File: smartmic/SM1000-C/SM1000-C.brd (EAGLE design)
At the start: 65 x 90 mm, 176 parts, among them CN1 HDR100-3, CN10 MJ-3523-SMT, CN11 HDR100-3, CN12 DF11-16DS, CN2 MOLEX-MINI-B-SMT, CN3 RASM712PX, CN4 RJ-45, CN5 MJ-3523-SMT, CN6 MJ-3523-SMT, CN7 MJ-3523-SMT, CN8 MJ-3523-SMT, CN9 MJ-3523-SMT, J1 JMP-2PIN, J3 JMP-2PIN, J4 JMP-2PIN, J5 JMP-2PIN, P1 TPAD50, P10 TPAD50, P11 TPAD50, P12 TPAD50, P13 TPAD50, P14 TPAD50, P15 TPAD50, P16 TPAD50, P17 TPAD50, P18 TPAD50, P19 TPAD50, P2 TPAD50, P20 TPAD50, P3 TPAD50, P4 TPAD50, P5 TPAD50, P6 TPAD50, P7 TPAD50, P8 TPAD50, P9 TPAD50, SW1 SW-BOURNS-7914S, SW2 SW-BOURNS-7914S, SW3 DPDT, SW4 SW-BOURNS-7914S, T1 SM-LP-5001, T2 SM-LP-5001, U1 STM32F405, U2 LD3985M33R, U3 STMPS2141, U4 EMIF02-USB03F2, U5 TPS54329E, U6 LMV341, U7 LMV341, U8 LM386M-1, U9 LMV341

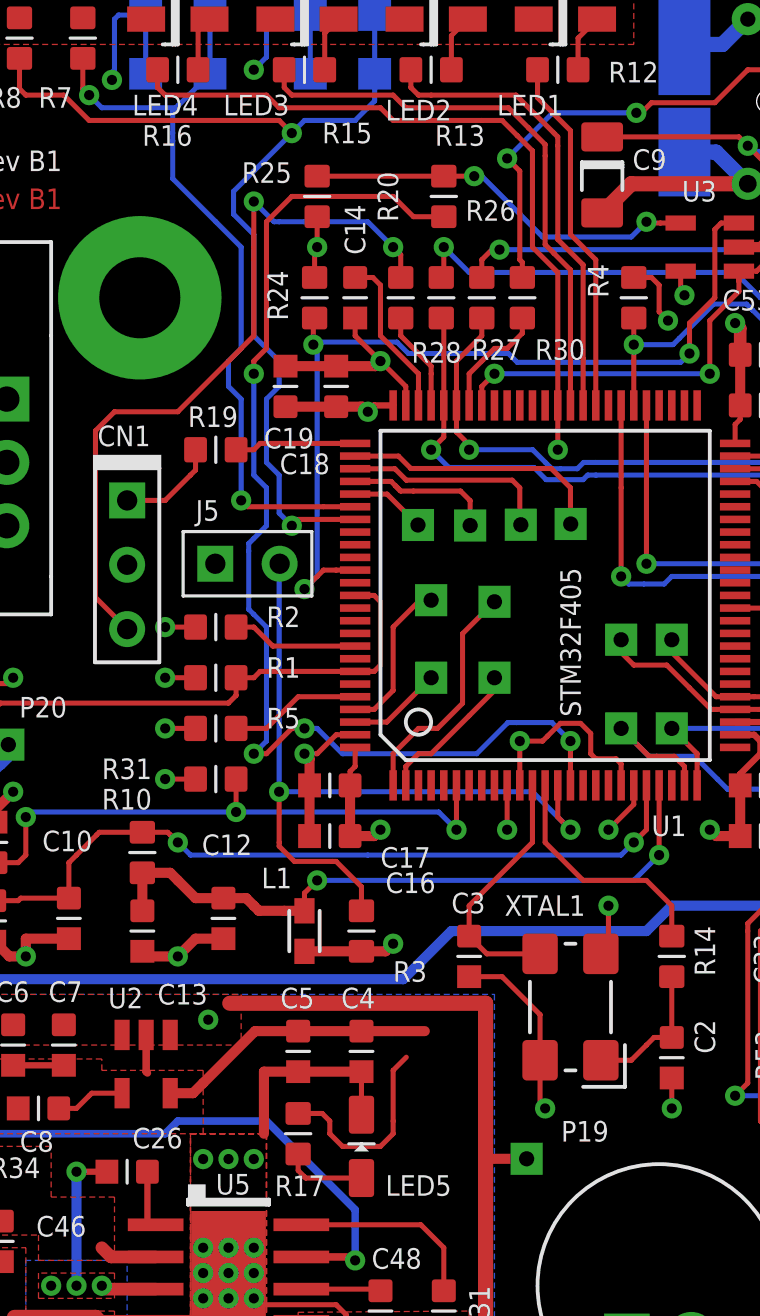
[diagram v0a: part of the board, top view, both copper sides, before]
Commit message: Verifying Change-Log-C items 1-15 RGB
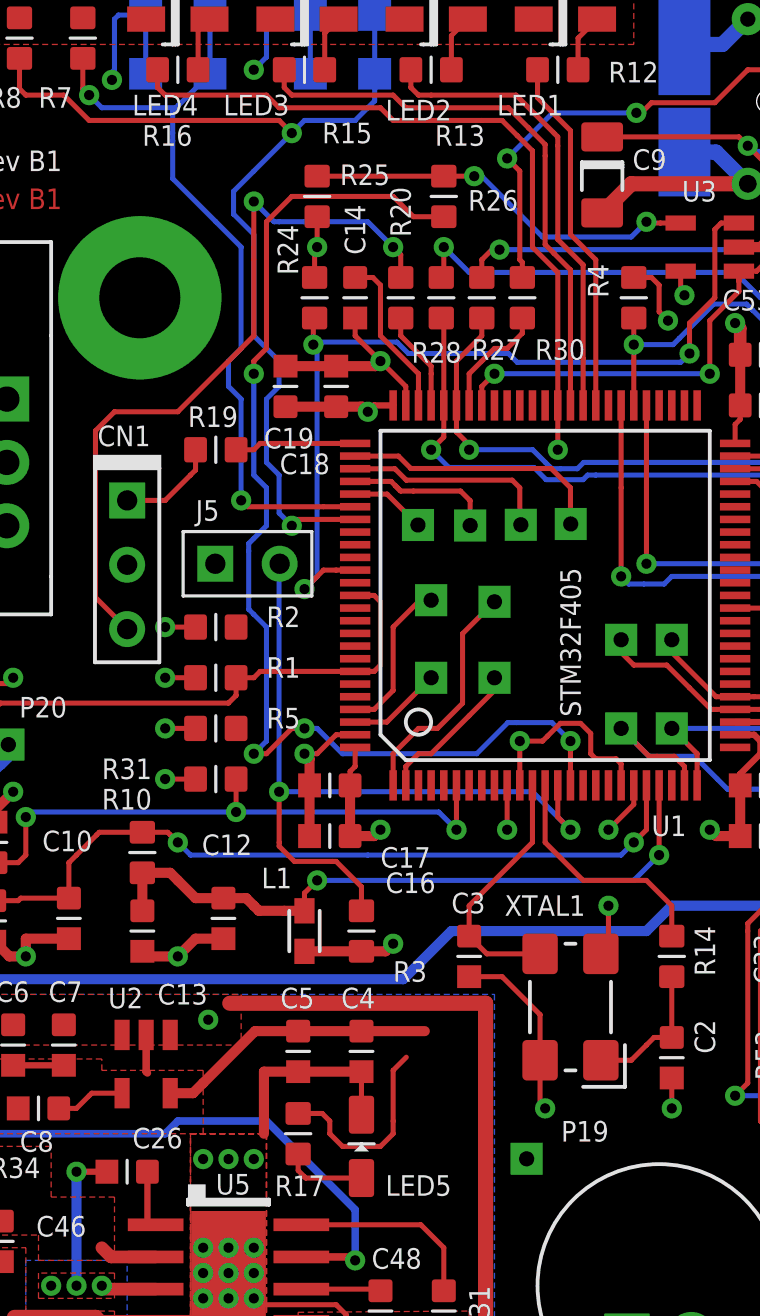
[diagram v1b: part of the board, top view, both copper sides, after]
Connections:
- removed net SCL: R2.2, U1.92
- removed net SDA: R5.2, U1.96
- net USART3_RX: now also R2.2
- net USART3_TX: now also R5.2
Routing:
- net SDA: track 5.22 -> 0.00 mm
- net SCL: track 5.01 -> 0.00 mm
- net +5V: track 96.6 -> 95.0 mm
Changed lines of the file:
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@@
 <layer number="14" name="Route14" color="1" fill="6" visible="no" active="no"/>
 <layer number="15" name="VDD" color="6" fill="1" visible="no" active="yes"/>
-<layer number="16" name="Bottom" color="1" fill="1" visible="yes" active="yes"/>
+<layer number="16" name="Bottom" color="1" fill="1" visible="no" active="yes"/>
 <layer number="17" name="Pads" color="2" fill="1" visible="yes" active="yes"/>
 <layer number="18" name="Vias" color="2" fill="1" visible="yes" active="yes"/>
@@
 <layer number="23" name="tOrigins" color="15" fill="1" visible="yes" active="yes"/>
 <layer number="24" name="bOrigins" color="15" fill="1" visible="no" active="yes"/>
-<layer number="25" name="tNames" color="7" fill="1" visible="no" active="yes"/>
+<layer number="25" name="tNames" color="7" fill="1" visible="yes" active="yes"/>
 <layer number="26" name="bNames" color="7" fill="1" visible="no" active="yes"/>
 <layer number="27" name="tValues" color="7" fill="1" visible="no" active="yes"/>
@@
 <layer number="203" name="BDIM" color="7" fill="1" visible="no" active="yes"/>
 <layer number="204" name="BRD-DIM" color="7" fill="1" visible="no" active="yes"/>
-<layer number="205" name="Speaker" color="7" fill="1" visible="yes" active="yes"/>
+<layer number="205" name="Speaker" color="7" fill="1" visible="no" active="yes"/>
 <layer number="250" name="Descript" color="3" fill="1" visible="no" active="no"/>
 <layer number="251" name="SMDround" color="12" fill="11" visible="no" active="no"/>
@@
 </element>
 <element name="R20" library="AA-ipc-7351-resistor" package="RESC1608X55N" value="22,1%" x="22.8" y="77.5" locked="yes" smashed="yes" rot="R90">
-<attribute name="NAME" x="22.7" y="80.5" size="0.8128" layer="25" rot="R90"/>
+<attribute name="NAME" x="23.2" y="79.9" size="0.8128" layer="25" rot="R90"/>
 </element>
 <element name="U2" library="_RoweTel" package="SOT23-5L" value="LD3985M33R" x="12.75" y="47.25" locked="yes" smashed="yes">
@@
 </element>
 <element name="R25" library="AA-ipc-7351-resistor" package="RESC1608X55N" value="10K,1%" x="19.5" y="81.5" locked="yes" smashed="yes" rot="R270">
-<attribute name="NAME" x="18.5" y="82.85" size="0.8128" layer="25" rot="R180"/>
+<attribute name="NAME" x="20.4" y="81.95" size="0.8128" layer="25"/>
 </element>
 <element name="R26" library="AA-ipc-7351-resistor" package="RESC1608X55N" value="0 Ohm" x="24.5" y="81.5" smashed="yes" rot="R90">
-<attribute name="NAME" x="25.361" y="80.539" size="0.8128" layer="25"/>
+<attribute name="NAME" x="25.461" y="80.939" size="0.8128" layer="25"/>
 </element>
 <element name="C9" library="_RoweTel" package="C1206-TANT" value="4.7uF,16V,TANT" x="30.75" y="82.35" locked="yes" smashed="yes" rot="R270">
@@
 </element>
 <element name="R24" library="AA-ipc-7351-resistor" package="RESC1608X55N" value="47K,1%" x="19.4" y="77.5" locked="yes" smashed="yes" rot="R270">
-<attribute name="NAME" x="18.35" y="76.6" size="0.8128" layer="25" rot="R90"/>
+<attribute name="NAME" x="18.75" y="78.4" size="0.8128" layer="25" rot="R90"/>
 </element>
 <element name="R46" library="_RoweTel" package="POT-3310C" value="100K" x="55.43" y="88.99" locked="yes" smashed="yes" rot="R90">
@@
 <wire x1="-30.3" y1="-49.5" x2="3.07" y2="6.26" width="0" layer="19" extent="1-1"/>
 </signal>
-<signal name="SCL">
-<contactref element="U1" pad="92"/>
-<contactref element="R2" pad="2"/>
-<wire x1="16.3" y1="64.5" x2="17" y2="64.5" width="0.2" layer="1"/>
-<wire x1="17" y1="64.5" x2="17.75" y2="63.75" width="0.2" layer="1"/>
-<wire x1="17.75" y1="63.75" x2="21" y2="63.75" width="0.2" layer="1"/>
-</signal>
-<signal name="SDA">
-<contactref element="U1" pad="96"/>
-<contactref element="R5" pad="2"/>
-<wire x1="21" y1="61.75" x2="18.75" y2="61.75" width="0.2" layer="1"/>
-<wire x1="18.75" y1="61.75" x2="17.5" y2="60.5" width="0.2" layer="1"/>
-<wire x1="17.5" y1="60.5" x2="16.3" y2="60.5" width="0.2" layer="1"/>
-</signal>
 <signal name="NRST">
 <contactref element="U1" pad="14"/>
@@
 <vertex x="1" y="1"/>
 </polygon>
-<contactref element="P19" pad="1"/>
 <wire x1="26.15" y1="43.5" x2="26.16" y2="43.51" width="0.4" layer="1"/>
-<wire x1="26.16" y1="43.51" x2="27.77" y2="43.51" width="0.4" layer="1"/>
 <wire x1="10.6" y1="49.65" x2="14.35" y2="49.65" width="0.4" layer="15"/>
 <via x="15.2" y="49" extent="1-16" drill="0.4"/>
 <wire x1="15.2" y1="49" x2="14.55" y2="49.65" width="0.4" layer="15"/>
 <wire x1="14.55" y1="49.65" x2="14.35" y2="49.65" width="0.4" layer="15"/>
+<contactref element="P19" pad="1"/>
+<wire x1="26.16" y1="43.51" x2="27.77" y2="43.51" width="0" layer="19" extent="1-1"/>
+<wire x1="15.2" y1="49" x2="16.05" y2="49.65" width="0" layer="19" extent="1-1"/>
+<wire x1="9.5" y1="48.8" x2="10.6" y2="49.65" width="0" layer="19" extent="1-15"/>
+<wire x1="13.7" y1="48.4" x2="14.35" y2="49.65" width="0" layer="19" extent="1-15"/>
+<wire x1="11.8" y1="48.4" x2="10.6" y2="49.65" width="0" layer="19" extent="1-15"/>
+<wire x1="7.5" y1="48.8" x2="9.5" y2="48.8" width="0" layer="19" extent="1-1"/>
+<wire x1="15.25" y1="28.25" x2="17.2" y2="29.5" width="0" layer="19" extent="1-1"/>
+<wire x1="5" y1="48.8" x2="7.5" y2="48.8" width="0" layer="19" extent="1-1"/>
+<wire x1="12.25" y1="28.25" x2="15.25" y2="28.25" width="0" layer="19" extent="1-1"/>
+<wire x1="15.3" y1="24.7" x2="15.25" y2="28.25" width="0" layer="19" extent="1-1"/>
+<wire x1="16.8" y1="24.7" x2="15.3" y2="24.7" width="0" layer="19" extent="1-1"/>
+<wire x1="10.8" y1="24.7" x2="12.25" y2="28.25" width="0" layer="19" extent="1-1"/>
+<wire x1="9.3" y1="24.7" x2="10.8" y2="24.7" width="0" layer="19" extent="1-1"/>
+<wire x1="5.95" y1="28.75" x2="9.3" y2="24.7" width="0" layer="19" extent="1-1"/>
 </signal>
 <signal name="N$12">
@@
 <wire x1="38.9" y1="68.9" x2="42.68" y2="68.9" width="0.2" layer="1"/>
 <wire x1="42.68" y1="68.9" x2="43.7" y2="69.92" width="0.2" layer="1"/>
+<contactref element="R2" pad="2"/>
+<wire x1="16.3" y1="64.5" x2="36" y2="70.75" width="0" layer="19" extent="1-1"/>
 </signal>
 <signal name="USART3_TX">
@@
 <wire x1="39.5" y1="68.4" x2="43.9" y2="68.4" width="0.2" layer="1"/>
 <wire x1="43.9" y1="68.4" x2="45" y2="69.5" width="0.2" layer="1"/>
+<contactref element="R5" pad="2"/>
+<wire x1="16.3" y1="60.5" x2="36" y2="70.25" width="0" layer="19" extent="1-1"/>
 </signal>
 <signal name="N$7">

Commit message: Update to reflect review of Change-Log-C.txt  RGB 09/08/2014
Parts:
- added C54: 1nF,16V, AA-ipc-7351-capacitor:CAPC1608X92N
- added R23: 10K,1%, AA-ipc-7351-resistor:RESC1608X55N
- R39: value 22.1K,1% -> 2.21K,1%
- moved R22 82.7 mm to (-5.00, 29.5)
- moved C36 38.7 mm to (67.6, 58.0)
- moved C12 34.4 mm to (-17.7, 45.0)
- moved C13 33.8 mm to (-20.4, 45.0)
- moved R10 29.4 mm to (-14.9, 45.1)
- moved L1 26.1 mm to (-6.00, 45.0)
- moved C10 20.2 mm to (-8.80, 45.0)
- moved C11 20.2 mm to (-11.8, 44.9)
- moved R21 3.54 mm to (-2.50, 50.5)
- moved R18 3.50 mm to (-2.50, 45.0)
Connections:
- removed net N$81: R47.3, R49.2
- new net N$13: R47.1, R49.2
- new net N$14: R23.2, R43.1, U6.3
- net AIN1: now also R23.1; no longer R43.1, U6.3
- net AIN2: now also C54.2, R42.1; no longer R42.3
- net N$41: now also C54.1, R42.3; no longer R42.1
- net N$82: now also R47.3; no longer R47.1
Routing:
- net N$50: track 67.7 -> 0.00 mm, vias 4 -> 0
- net N$9: track 50.9 -> 0.00 mm, vias 1 -> 0
- net N$4: track 30.2 -> 2.46 mm, vias 2 -> 1
- net N$5: track 26.6 -> 2.75 mm, vias 2 -> 1
- net N$11: track 22.4 -> 0.00 mm, vias 1 -> 0
- net GND: track 228.2 -> 220.8 mm, vias 44 -> 42
- net N$81: track 4.89 -> 0.00 mm
- net AIN1: track 35.6 -> 31.5 mm
- net N$41: track 22.7 -> 18.7 mm
- net VDD: track 148.4 -> 146.2 mm
- net AIN2: track 60.6 -> 58.4 mm
- net N$82: track 4.44 -> 2.44 mm
- net N$14: track 0.00 -> 1.69 mm

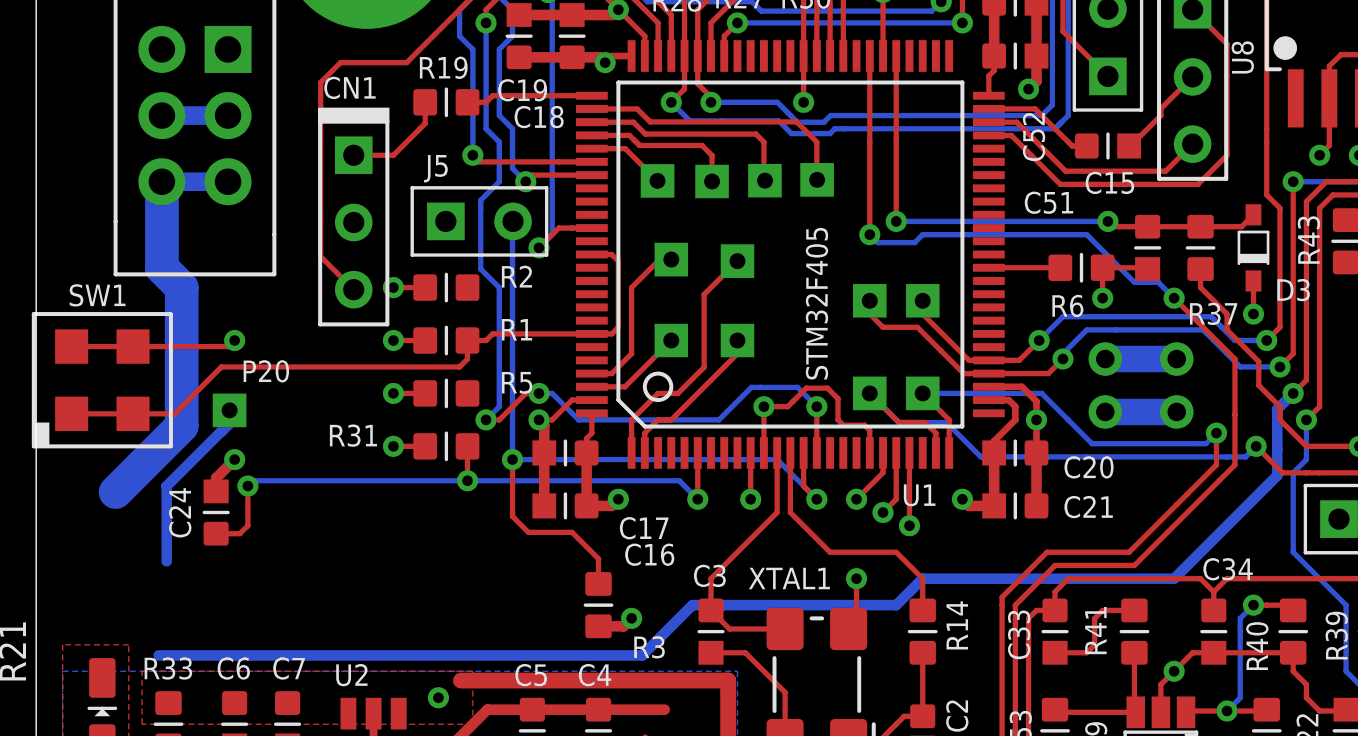
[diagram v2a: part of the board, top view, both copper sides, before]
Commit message: Update SNN with Change-Log-C.txt changes. RGB 09/10/2014
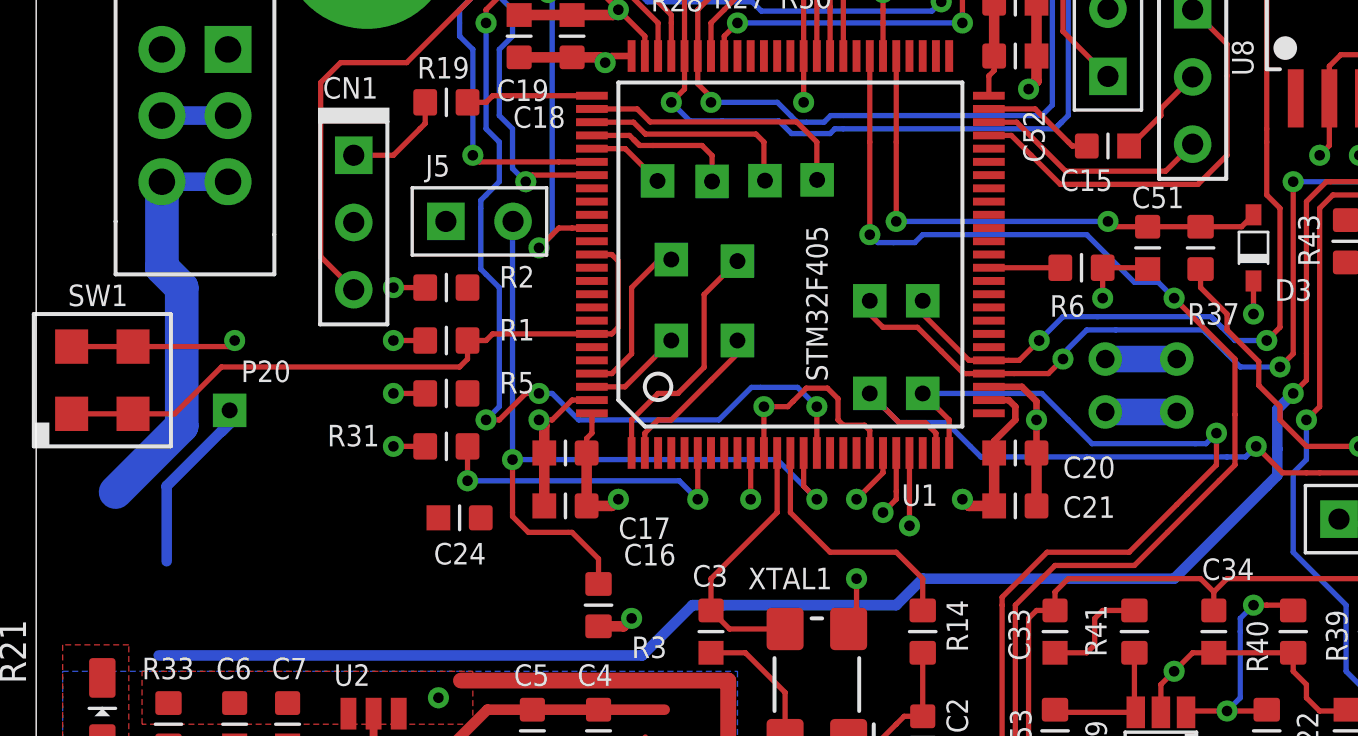
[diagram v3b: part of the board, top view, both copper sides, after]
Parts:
- C40: value 100nF,25V -> 47nF,25V
- moved C24 9.20 mm to (16.0, 55.8), turned to 180 degrees
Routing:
- net N$2: track 23.2 -> 12.0 mm, vias 3 -> 2
- net GND: track 220.8 -> 219.3 mm, vias 42 -> 41
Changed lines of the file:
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@@
 <attribute name="NAME" x="48.43" y="30.5" size="0.8128" layer="25" ratio="10"/>
 </element>
-<element name="C24" library="AA-ipc-7351-capacitor" package="CAPC1608X92N" value="1uF,16V" x="6.8" y="56" locked="yes" smashed="yes" rot="R90">
-<attribute name="NAME" x="5.85" y="55" size="0.8128" layer="25" ratio="10" rot="R90"/>
-<attribute name="VALUE" x="8.8375" y="54.75" size="1" layer="27" font="vector" ratio="10" rot="R90"/>
+<element name="C24" library="AA-ipc-7351-capacitor" package="CAPC1608X92N" value="1uF,16V" x="16" y="55.8" smashed="yes" rot="R180">
+<attribute name="NAME" x="17" y="54.85" size="0.8128" layer="25" ratio="10" rot="R180"/>
+<attribute name="VALUE" x="17.25" y="57.8375" size="1" layer="27" font="vector" ratio="10" rot="R180"/>
 </element>
 <element name="C21" library="AA-ipc-7351-capacitor" package="CAPC1608X92N" value="10nF,16V" x="37" y="56.25" locked="yes" smashed="yes" rot="R180">
@@
 </element>
 <element name="C15" library="AA-ipc-7351-capacitor" package="CAPC1608X92N" value="2.2uF,16V" x="40.5" y="69.85" locked="yes" smashed="yes">
-<attribute name="NAME" x="39.6" y="68.05" size="0.8128" layer="25" ratio="10"/>
+<attribute name="NAME" x="38.7" y="68.15" size="0.8128" layer="25" ratio="10"/>
 <attribute name="VALUE" x="39.025" y="67.5625" size="1" layer="27" font="vector" ratio="10"/>
 </element>
@@
 <attribute name="VALUE" x="50.2875" y="79.75" size="1" layer="27" font="vector" ratio="10" rot="R90"/>
 </element>
-<element name="C40" library="AA-ipc-7351-capacitor" package="CAPC1608X92N" value="100nF,25V" x="55.75" y="81" locked="yes" smashed="yes" rot="R90">
+<element name="C40" library="AA-ipc-7351-capacitor" package="CAPC1608X92N" value="47nF,25V" x="55.75" y="81" locked="yes" smashed="yes" rot="R90">
 <attribute name="NAME" x="56.7" y="82.1" size="0.8128" layer="25" ratio="10" rot="R270"/>
 <attribute name="VALUE" x="57.7875" y="79.75" size="1" layer="27" font="vector" ratio="10" rot="R90"/>
@@
 </element>
 <element name="C51" library="AA-ipc-7351-capacitor" package="CAPC1608X92N" value="100nF,16V" x="42" y="66" locked="yes" smashed="yes" rot="R270">
-<attribute name="NAME" x="37.3" y="67.3" size="0.8128" layer="25" font="vector" ratio="10"/>
+<attribute name="NAME" x="41.4" y="67.5" size="0.8128" layer="25" font="vector" ratio="10"/>
 <attribute name="VALUE" x="39.9625" y="67.25" size="1" layer="27" font="vector" ratio="10" rot="R270"/>
 </element>
@@
 <wire x1="16.3" y1="57.2" x2="24.3" y2="57.2" width="0.2" layer="16"/>
 <wire x1="24.3" y1="57.2" x2="25" y2="56.5" width="0.2" layer="16"/>
-<wire x1="16.3" y1="57.2" x2="8.2" y2="57.2" width="0.2" layer="16"/>
-<wire x1="8.2" y1="57.2" x2="8" y2="57" width="0.2" layer="16"/>
-<via x="8" y="57" extent="1-16" drill="0.4"/>
-<wire x1="6.8" y1="55.2" x2="7.7" y2="55.2" width="0.2" layer="1"/>
-<wire x1="7.7" y1="55.2" x2="8" y2="55.5" width="0.2" layer="1"/>
-<wire x1="8" y1="55.5" x2="8" y2="57" width="0.2" layer="1"/>
+<wire x1="16.8" y1="55.8" x2="16.3" y2="57.2" width="0" layer="19" extent="1-1"/>
 </signal>
 <signal name="N$5">
@@
 <wire x1="20.25" y1="74.8" x2="21.8" y2="74.8" width="0.4" layer="1"/>
 <wire x1="21.8" y1="74.8" x2="22" y2="75" width="0.4" layer="1"/>
-<wire x1="6.8" y1="56.8" x2="6.8" y2="57.3" width="0.4" layer="1"/>
-<wire x1="6.8" y1="57.3" x2="7.5" y2="58" width="0.4" layer="1"/>
-<via x="7.5" y="58" extent="1-16" drill="0.4" diameter="0.8"/>
 <wire x1="14.7" y1="62.5" x2="13.5" y2="62.5" width="0.2" layer="1"/>
 <via x="13.5" y="62.5" extent="1-16" drill="0.4" diameter="0.8"/>
@@
 <contactref element="C49" pad="2"/>
 <contactref element="R22" pad="1"/>
-<wire x1="3.07" y1="6.26" x2="-5.8" y2="29.5" width="0" layer="19" extent="1-1"/>
+<wire x1="39.96" y1="18.25" x2="51.96" y2="18.25" width="0" layer="19" extent="1-1"/>
+<wire x1="63.5" y1="10.5" x2="51.96" y2="18.25" width="0" layer="19" extent="1-2"/>
+<wire x1="15.2" y1="55.8" x2="19.2" y2="56.25" width="0" layer="19" extent="1-1"/>
 <wire x1="-5.7" y1="58" x2="2.5" y2="49.75" width="0" layer="19" extent="1-1"/>
 <wire x1="-8.8" y1="44.2" x2="1.9" y2="39.5" width="0" layer="19" extent="1-1"/>
@@
 <wire x1="-17.7" y1="44.2" x2="-11.75" y2="44.1" width="0" layer="19" extent="1-1"/>
 <wire x1="-20.4" y1="44.2" x2="-17.7" y2="44.2" width="0" layer="19" extent="1-1"/>
-<wire x1="51.96" y1="18.25" x2="63.5" y2="10.5" width="0" layer="19" extent="1-2"/>
-<wire x1="39.96" y1="18.25" x2="51.96" y2="18.25" width="0" layer="19" extent="1-1"/>
+<wire x1="-5.8" y1="29.5" x2="1.9" y2="39.5" width="0" layer="19" extent="1-1"/>
 </signal>
 <signal name="NRST">
@@
 <wire x1="38.8" y1="63.4" x2="37.9" y2="62.5" width="0.2" layer="16"/>
 <contactref element="R22" pad="2"/>
-<wire x1="-4.2" y1="29.5" x2="35.25" y2="61.75" width="0" layer="19" extent="1-1"/>
+<wire x1="-4.2" y1="29.5" x2="33.5" y2="63.5" width="0" layer="19" extent="1-1"/>
 </signal>
 <signal name="DAC1_OUT">
@@
 <contactref element="R43" pad="2"/>
 <contactref element="C36" pad="1"/>
-<wire x1="67.6" y1="59.5" x2="49.5" y2="65.45" width="0" layer="19" extent="1-1"/>
+<wire x1="49.5" y1="65.45" x2="67.6" y2="59.5" width="0" layer="19" extent="1-1"/>
 </signal>
 <signal name="N$63">
@@
 <contactref element="R52" pad="2"/>
 <contactref element="C36" pad="2"/>
-<wire x1="67.6" y1="56.5" x2="59" y2="54.46" width="0" layer="19" extent="1-1"/>
+<wire x1="59" y1="54.46" x2="67.6" y2="56.5" width="0" layer="19" extent="1-1"/>
 </signal>
 <signal name="PE0">
